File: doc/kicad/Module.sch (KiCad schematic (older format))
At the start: 20 parts, among them J20 Conn_01x05, J21 Conn_01x05, J22 Prog, J23 Conn_01x05, J24 Conn_01x05, J25 Conn_01x04, J26 Conn_01x04, J27 Conn_01x05, Q2 BC548, Q3 BC548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

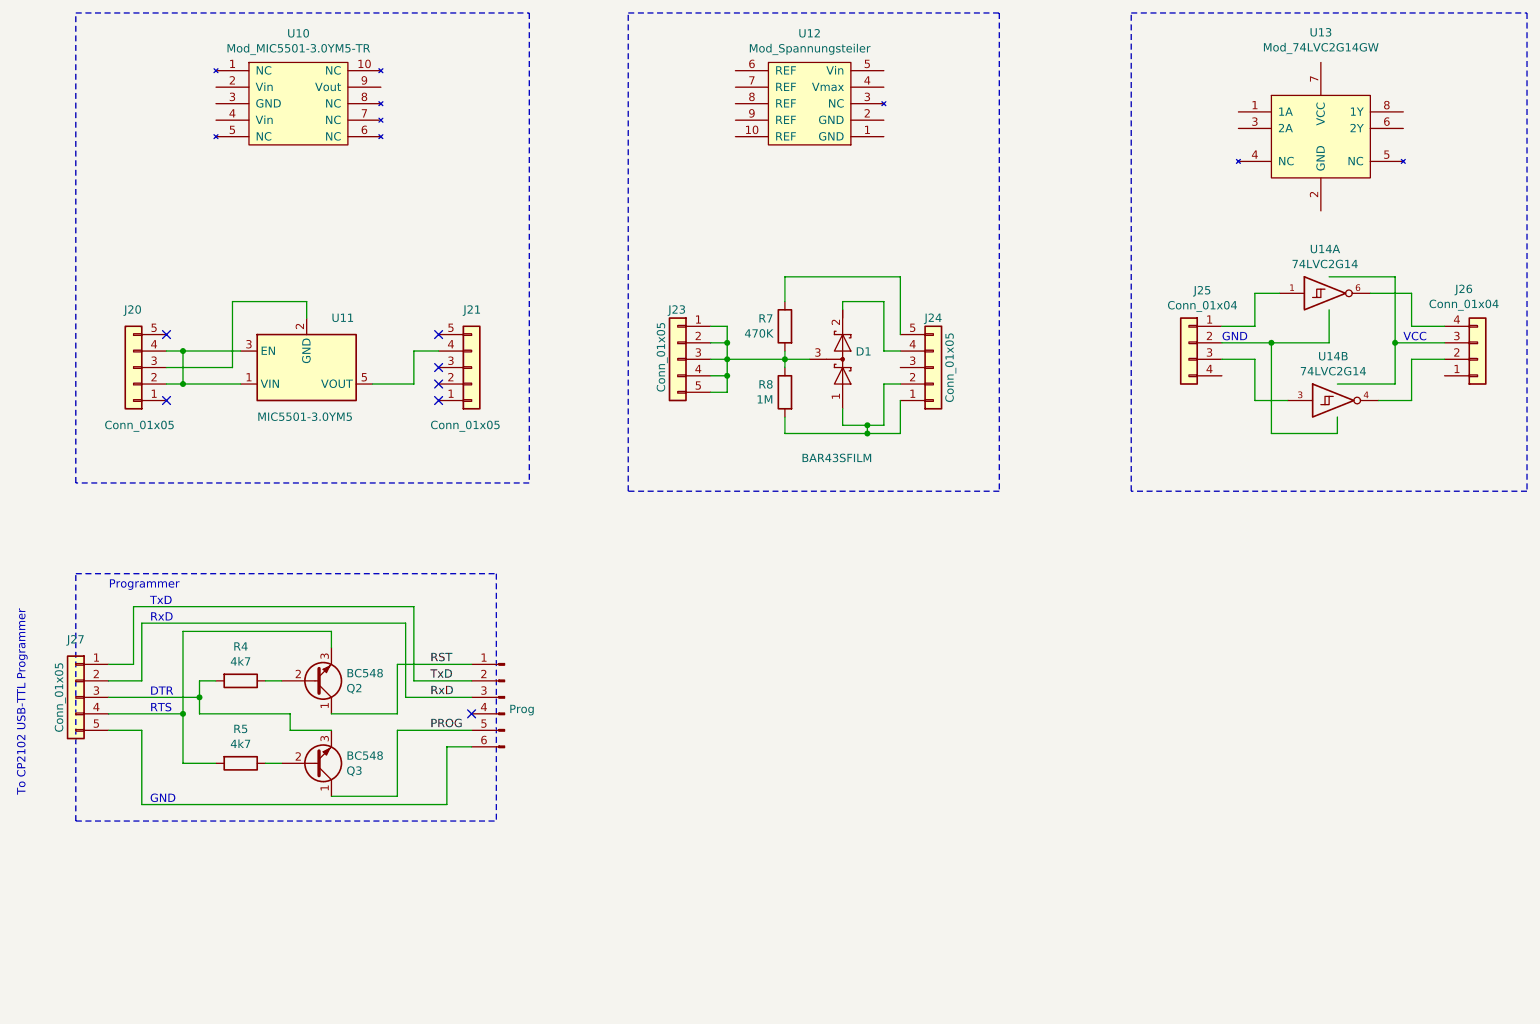
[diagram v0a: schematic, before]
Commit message: Stable without Solar monitor
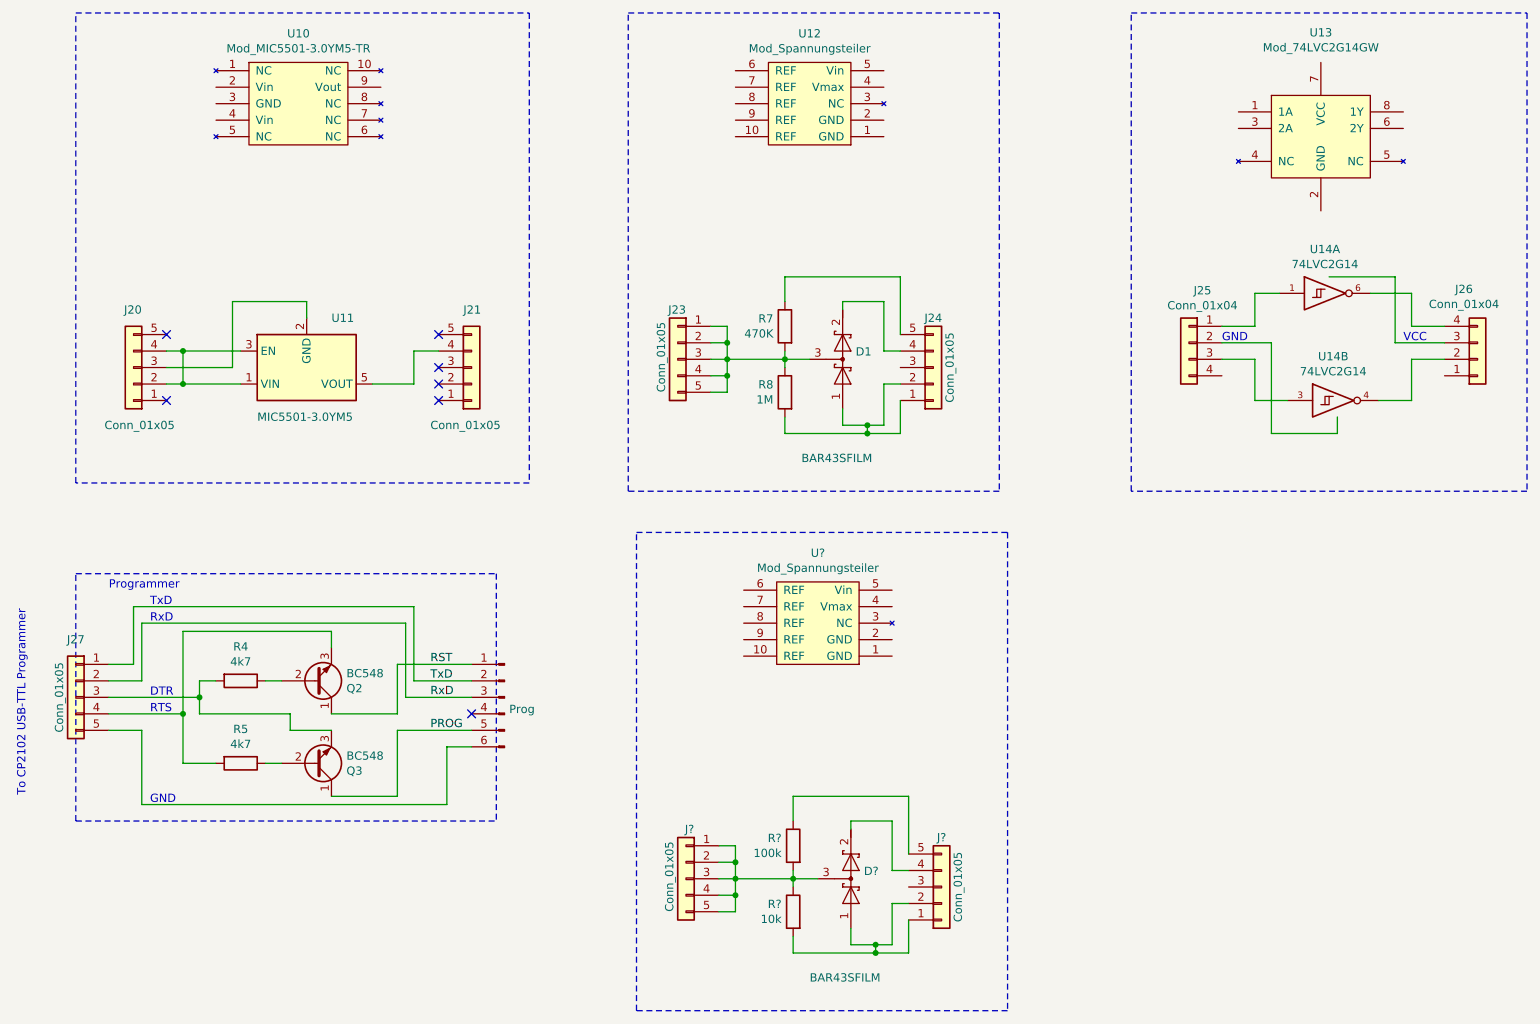
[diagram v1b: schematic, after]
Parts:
- added D?: BAR43SFILM, symbol ESP:BAR43SFILM
- added J? (x2): Conn_01x05, Socket_Strips:Socket_Strip_Straight_1x05_Pitch2.54mm, symbol Connector_Generic:Conn_01x05
- added R?: 100k, symbol Device:R
- added R?: 10k, symbol Device:R
- added U?: Mod_Spannungsteiler, Module:Mod_SOT23_TO_10DIL, symbol Module:Mod_Spannungsteiler
- D1: footprint TO_SOT_Packages_SMD:SOT-23 -> (none)
- R7, R8: footprint Resistors_SMD:R_0805 -> (none)
- U11: footprint TO_SOT_Packages_SMD:SOT-23-5 -> (none)
- U14: footprint TO_SOT_Packages_SMD:SOT-363_SC-70-6 -> (none)
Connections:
- new net: D?.1 (A), J?.1 (Pin_1), J?.2 (Pin_2), R?.2
- new net: D?.2 (K), J?.4 (Pin_4)
- new net: D?.3 (AK), J?.1 (Pin_1), J?.2 (Pin_2), J?.3 (Pin_3), J?.4 (Pin_4), J?.5 (Pin_5), R?.1, R?.2
- new net: J?.5 (Pin_5), R?.1
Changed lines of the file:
@@
 EESchema Schematic File Version 4
 LIBS:WeatherStation-cache
-LIBS:Module-cache
 EELAYER 30 0
 EELAYER END
@@
 F 0 "U11" H 2750 3000 50  0000 L CNN
 F 1 "MIC5501-3.0YM5" H 2300 3600 50  0000 L CNN
-F 2 "TO_SOT_Packages_SMD:SOT-23-5" H 2600 2900 50  0001 C CNN
+F 2 "" H 2600 2900 50  0001 C CNN
 F 3 "http://ww1.microchip.com/downloads/en/DeviceDoc/MIC550X.pdf" H 2350 3550 50  0001 C CNN
 	1    2600 3300
@@
 F 0 "D1" V 5896 3329 50  0000 L CNN
 F 1 "BAR43SFILM" V 5250 3000 50  0000 L CNN
-F 2 "TO_SOT_Packages_SMD:SOT-23" H 5850 3250 50  0001 C CNN
+F 2 "" H 5850 3250 50  0001 C CNN
 F 3 "~" H 5850 3250 50  0001 C CNN
 	1    5850 3250
@@
 F 0 "R7" H 5570 3096 50  0000 L CNN
 F 1 "470K" H 5570 3005 50  0000 L CNN
-F 2 "Resistors_SMD:R_0805" V 5430 3050 50  0001 C CNN
+F 2 "" V 5430 3050 50  0001 C CNN
 F 3 "~" H 5500 3050 50  0001 C CNN
 	1    5500 3050
@@
 F 0 "R8" H 5570 3496 50  0000 L CNN
 F 1 "1M" H 5570 3405 50  0000 L CNN
-F 2 "Resistors_SMD:R_0805" V 5430 3450 50  0001 C CNN
+F 2 "" V 5430 3450 50  0001 C CNN
 F 3 "~" H 5500 3450 50  0001 C CNN
 	1    5500 3450
@@
 F 0 "U14" H 8775 3117 50  0000 C CNN
 F 1 "74LVC2G14" H 8775 3026 50  0000 C CNN
-F 2 "TO_SOT_Packages_SMD:SOT-363_SC-70-6" H 8800 2850 50  0001 C CNN
+F 2 "" H 8800 2850 50  0001 C CNN
 F 3 "https://www.ti.com/lit/ds/symlink/sn74lvc2g14.pdf" H 8800 2850 50  0001 C CNN
 	1    8800 2850
@@
 F 0 "U14" H 8825 3767 50  0000 C CNN
 F 1 "74LVC2G14" H 8825 3676 50  0000 C CNN
-F 2 "TO_SOT_Packages_SMD:SOT-363_SC-70-6" H 8850 3500 50  0001 C CNN
+F 2 "" H 8850 3500 50  0001 C CNN
 F 3 "https://www.ti.com/lit/ds/symlink/sn74lvc2g14.pdf" H 8850 3500 50  0001 C CNN
 	2    8850 3500
@@
 	8150 3150 8450 3150
 Wire Wire Line
-	8800 3150 8800 2950
-Wire Wire Line
 	8450 3150 8450 3700
 Wire Wire Line
@@
 Wire Wire Line
 	8850 3700 8850 3600
-Connection ~ 8450 3150
-Wire Wire Line
-	8450 3150 8800 3150
-Wire Wire Line
-	8850 3400 9200 3400
-Wire Wire Line
-	9200 3400 9200 3150
 Wire Wire Line
 	9200 3150 9500 3150
@@
 Wire Wire Line
 	9200 2750 8800 2750
-Connection ~ 9200 3150
 Text Notes 9250 3150 0    50   ~ 0
 VCC
@@
 Wire Wire Line
 	1550 4750 3250 4750
+$Comp
+L ESP:BAR43SFILM D?
+U 1 1 5D91C532
+P 5900 6400
+F 0 "D?" V 5946 6479 50  0000 L CNN
+F 1 "BAR43SFILM" V 5300 6150 50  0000 L CNN
+F 2 "" H 5900 6400 50  0001 C CNN
+F 3 "~" H 5900 6400 50  0001 C CNN
+	1    5900 6400
+	0    1    -1   0
+$EndComp
+$Comp
+L Device:R R?
+U 1 1 5D91C538
+P 5550 6200
+F 0 "R?" H 5620 6246 50  0000 L CNN
+F 1 "100k" H 5620 6155 50  0000 L CNN
+F 2 "" V 5480 6200 50  0001 C CNN
+F 3 "~" H 5550 6200 50  0001 C CNN
+	1    5550 6200
+	-1   0    0    -1
+$EndComp
+$Comp
+L Device:R R?
+U 1 1 5D91C53E
+P 5550 6600
+F 0 "R?" H 5620 6646 50  0000 L CNN
+F 1 "10k" H 5620 6555 50  0000 L CNN
+F 2 "" V 5480 6600 50  0001 C CNN
+F 3 "~" H 5550 6600 50  0001 C CNN
+	1    5550 6600
+	-1   0    0    -1
+$EndComp
+Wire Wire Line
+	5700 6400 5550 6400
+Wire Wire Line
+	5550 6400 5550 6350
+Wire Wire Line
+	5550 6450 5550 6400
+Connection ~ 5550 6400
+$Comp
+L Connector_Generic:Conn_01x05 J?
+U 1 1 5D91C548
+P 4900 6400
+F 0 "J?" H 4850 6700 50  0000 L CNN
+F 1 "Conn_01x05" V 5000 6200 50  0000 L CNN
+F 2 "Socket_Strips:Socket_Strip_Straight_1x05_Pitch2.54mm" H 4900 6400 50  0001 C CNN
+F 3 "~" H 4900 6400 50  0001 C CNN
+	1    4900 6400
+	-1   0    0    -1
+$EndComp
+$Comp
+L Connector_Generic:Conn_01x05 J?
+U 1 1 5D91C54E
+P 6450 6450
+F 0 "J?" H 6450 6150 50  0000 C CNN
+F 1 "Conn_01x05" V 6550 6450 50  0000 C CNN
+F 2 "Socket_Strips:Socket_Strip_Straight_1x05_Pitch2.54mm" H 6450 6450 50  0001 C CNN
+F 3 "~" H 6450 6450 50  0001 C CNN
+	1    6450 6450
+	1    0    0    1
+$EndComp
+Wire Wire Line
+	5550 6400 5200 6400
+Wire Wire Line
+	5200 6400 5200 6300
+Wire Wire Line
+	5200 6200 5100 6200
+Connection ~ 5200 6400
+Wire Wire Line
+	5200 6400 5100 6400
+Wire Wire Line
+	5200 6400 5200 6500
+Wire Wire Line
+	5200 6600 5100 6600
+Wire Wire Line
+	5200 6500 5100 6500
+Connection ~ 5200 6500
+Wire Wire Line
+	5200 6500 5200 6600
+Wire Wire Line
+	5200 6300 5100 6300
+Connection ~ 5200 6300
+Wire Wire Line
+	5200 6300 5200 6200
+Wire Wire Line
+	6250 6250 6250 5900
+Wire Wire Line
+	6250 5900 5550 5900
+Wire Wire Line
+	5550 5900 5550 6050
+Wire Wire Line
+	6250 6350 6150 6350
+Wire Wire Line
+	6150 6350 6150 6050
+Wire Wire Line
+	6150 6050 5900 6050
+Wire Wire Line
+	5900 6050 5900 6100
+Wire Wire Line
+	6250 6550 6150 6550
+Wire Wire Line
+	6150 6550 6150 6800
+Wire Wire Line
+	6150 6800 6050 6800
+Wire Wire Line
+	5900 6800 5900 6700
+Wire Wire Line
+	6250 6650 6250 6850
+Wire Wire Line
+	6250 6850 6050 6850
+Wire Wire Line
+	5550 6850 5550 6750
+Wire Wire Line
+	6050 6850 6050 6800
+Wire Wire Line
+	6050 6850 5550 6850
+Wire Wire Line
+	6050 6800 5900 6800
+Connection ~ 6050 6800
+Connection ~ 6050 6850
+$Comp
+L Module:Mod_Spannungsteiler U?
+U 1 1 5D91C574
+P 5750 4850
+F 0 "U?" H 5700 5275 50  0000 C CNN
+F 1 "Mod_Spannungsteiler" H 5700 5184 50  0000 C CNN
+F 2 "Module:Mod_SOT23_TO_10DIL" H 5650 4450 50  0001 C CNN
+F 3 "" H 5550 4850 50  0001 C CNN
+	1    5750 4850
+	1    0    0    -1
+$EndComp
+Wire Notes Line
+	4600 4300 6850 4300
+Wire Notes Line
+	6850 4300 6850 7200
+Wire Notes Line
+	6850 7200 4600 7200
+Wire Notes Line
+	4600 7200 4600 4300
 $EndSCHEMATC

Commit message: Fixed WiFi freeze (ADC_2/Int Problems). Optimize Solar MPPT.
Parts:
- U12: value Mod_Spannungsteiler -> Mod_Divider_BAT
- U?: value Mod_Spannungsteiler -> Mod_Divider_Solar
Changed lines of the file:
@@
 P 5700 1700
 F 0 "U12" H 5650 2125 50  0000 C CNN
-F 1 "Mod_Spannungsteiler" H 5650 2034 50  0000 C CNN
+F 1 "Mod_Divider_BAT" H 5650 2034 50  0000 C CNN
 F 2 "Module:Mod_SOT23_TO_10DIL" H 5600 1300 50  0001 C CNN
 F 3 "" H 5500 1700 50  0001 C CNN
@@
 P 5750 4850
 F 0 "U?" H 5700 5275 50  0000 C CNN
-F 1 "Mod_Spannungsteiler" H 5700 5184 50  0000 C CNN
+F 1 "Mod_Divider_Solar" H 5700 5184 50  0000 C CNN
 F 2 "Module:Mod_SOT23_TO_10DIL" H 5650 4450 50  0001 C CNN
 F 3 "" H 5550 4850 50  0001 C CNN
